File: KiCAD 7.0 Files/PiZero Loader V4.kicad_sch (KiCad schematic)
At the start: 30 parts, among them J1 RPi_GPIO, J2 Conn_01x30, J3 Conn_01x30, Q1 2N2222, U1 74HCT165, U2 74HCT157, U3 74HCT157, U4 74HCT157

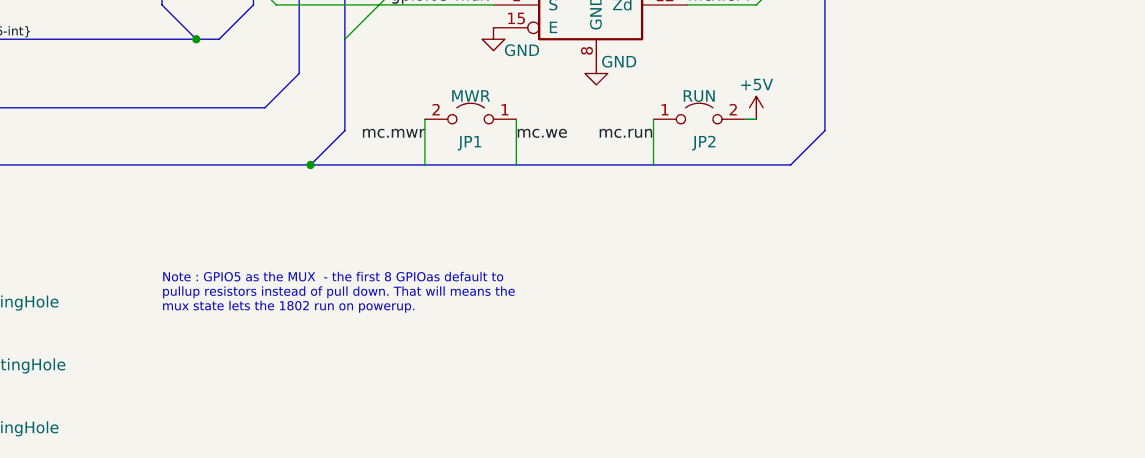
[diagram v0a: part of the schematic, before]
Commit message: added warning not to install JP1
if JP1 is installed and the front panel READ/WRTIE swtich is set to the READ position then the 1802 /MWR pin gets shorted to +5V
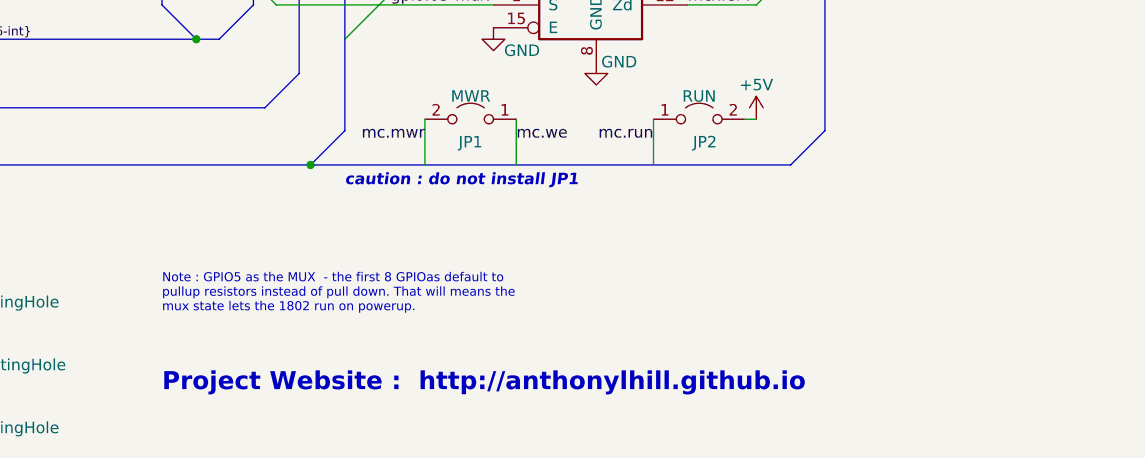
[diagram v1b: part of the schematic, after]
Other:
- note added: "Project Website : http://anthonylhill.github.io"
- note added: "caution : do not install JP1"
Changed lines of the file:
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@@
     (effects (font (size 2 2) (thickness 0.4) bold (color 255 0 0 1)) (justify left bottom))
+  )
+  (text "caution : do not install JP1" (at 181.61 163.83 0)
+    (effects (font (size 1.27 1.27) (thickness 0.254) bold italic (color 255 0 0 1)) (justify left bottom))
   )
   (text "GND\nOUT0\nOUT1\nOUT2\nOUT3\nOUT4\nOUT5\nOUT6\nOUT7\n/WE\n/MWR\nQ\nRUN\n+5V\nIN7\nIN6\nIN5\nIN4\nIN3\nIN2\nIN1\nIN0\n/INT\n/EF1\n/EF2\n/EF3\n/EF4\n/CLEAR\n/WAIT\nGND\n"
@@
     (effects (font (size 1.58 1.58)) (justify left bottom))
   )
+  (text "Project Website :  http://anthonylhill.github.io" (at 161.29 186.69 0)
+    (effects (font (face "Lucida Console") (size 2 2) (thickness 0.254) bold (color 205 0 0 1)) (justify left bottom))
+  )
   (text "Note : GPIO5 as the MUX  - the first 8 GPIOas default to \npullup resistors instead of pull down. That will means the \nmux state lets the 1802 run on powerup."

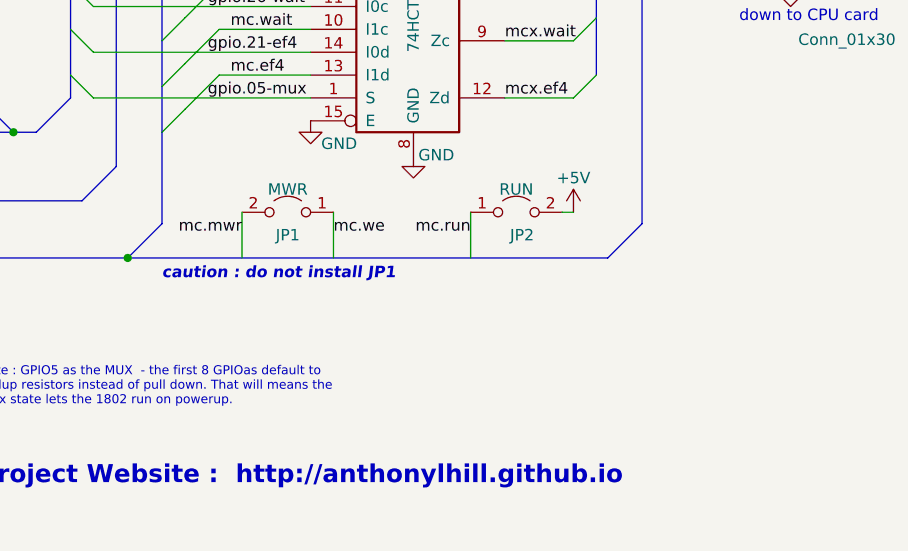
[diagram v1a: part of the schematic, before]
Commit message: JP1 & JP2 assembly instructions changed
= added wording to the assembly instructions and schematic stating that JP1 and JP2 are only for use with a standalone CPU card (i.e. when not using the MC Front Panel card).
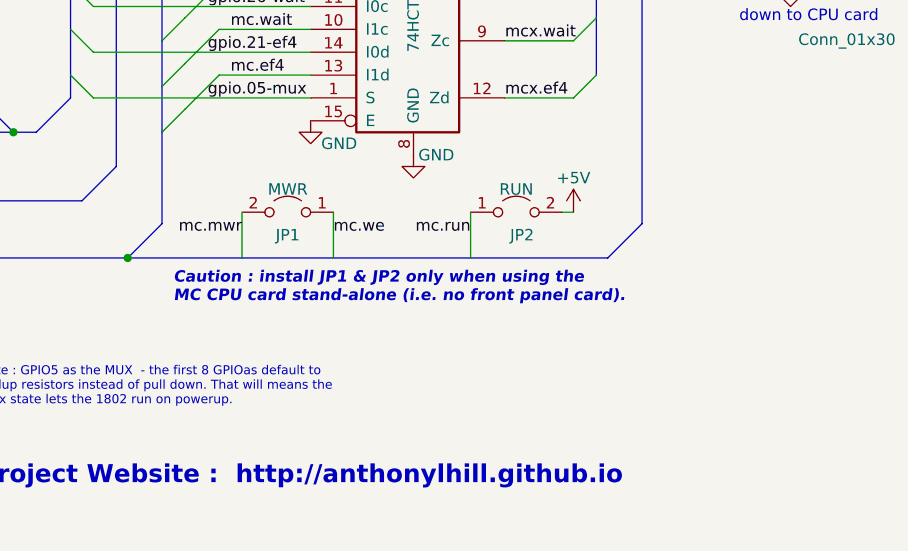
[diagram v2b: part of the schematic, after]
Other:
- note added: "Caution : install JP1 & JP2 only when using the MC CPU card stand-alone (i.e. no front panel card)."
- note removed: "caution : do not install JP1"
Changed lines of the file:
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@@
   (title_block
     (title "PiZero 1802 Membership Card Loader")
-    (date "2023-05-18")
-    (rev "4c")
+    (date "2023-12-26")
+    (rev "4d")
   )
   (junction (at 31.75 58.42) (diameter 0) (color 0 0 0 0)
@@
     (effects (font (size 2 2) (thickness 0.4) bold (color 255 0 0 1)) (justify left bottom))
   )
-  (text "caution : do not install JP1" (at 181.61 163.83 0)
+  (text "Caution : install JP1 & JP2 only when using the \nMC CPU card stand-alone (i.e. no front panel card)."
+    (at 182.88 166.37 0)
     (effects (font (size 1.27 1.27) (thickness 0.254) bold italic (color 255 0 0 1)) (justify left bottom))
   )
